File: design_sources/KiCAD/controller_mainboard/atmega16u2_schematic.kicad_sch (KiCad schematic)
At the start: 24 parts, among them J17 01x05_Socket, J18 02x02_pinheader, J19 02x03_pinheader, U2 ATmega16U2-M, Y2 16MHz

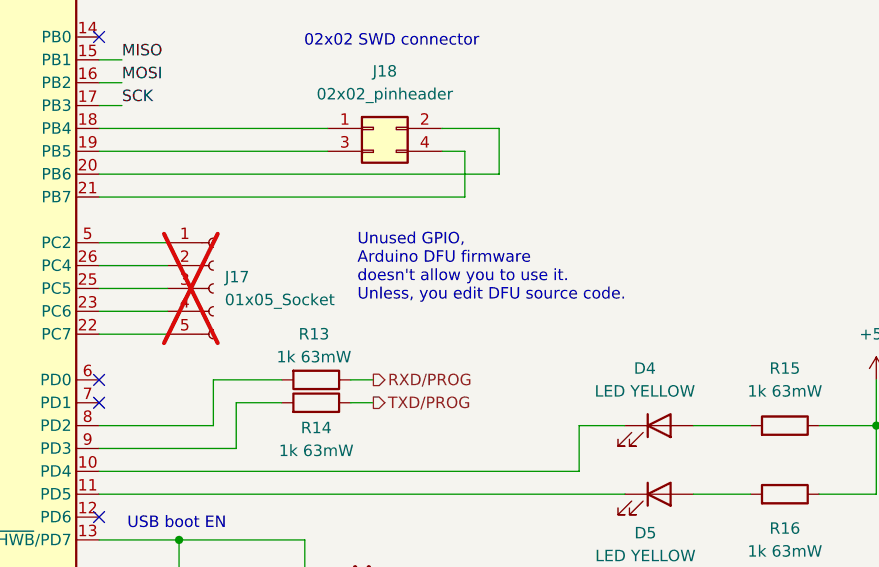
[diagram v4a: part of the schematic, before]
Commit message: Slight schematic adjustments and continue on draft pcb layout
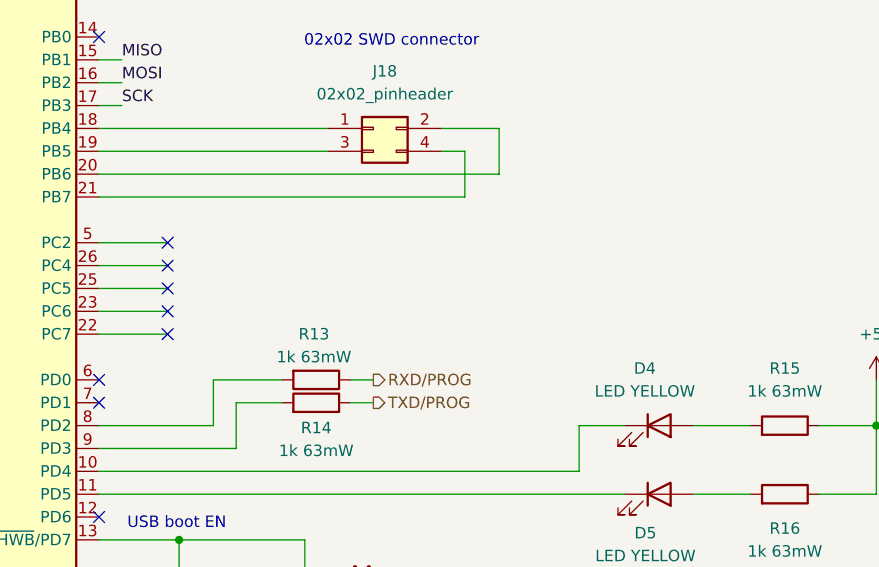
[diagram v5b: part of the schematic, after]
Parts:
- removed J17: 01x05_Socket, Connector_PinSocket_2.54mm:PinSocket_1x05_P2.54mm_Vertical, symbol Connector:Conn_01x05_Socket
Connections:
- no-connect marks 4 -> 9
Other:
- note removed: "Unused GPIO, Arduino DFU firmware doesn't allow you to use it. Unless, you edit DFU source code."
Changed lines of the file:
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@@
-		)
-	)
-	(text "Unused GPIO,\nArduino DFU firmware \ndoesn't allow you to use it.\nUnless, you edit DFU source code."
-		(exclude_from_sim no)
-		(at 148.082 96.774 0)
-		(effects
-			(font
-				(size 1.27 1.27)
-			)
-			(justify left)
 		)
 	)
@@
 	)
 	(no_connect
+		(at 127 101.6)
+	)
+	(no_connect
+		(at 127 93.98)
+	)
+	(no_connect
 		(at 119.38 124.46)
+	)
+	(no_connect
+		(at 127 104.14)
+	)
+	(no_connect
+		(at 127 96.52)
+	)
+	(no_connect
+		(at 127 99.06)
 	)
 	(wire
@@
 					(unit 1)
 				)
-			)
-		)
-	)
-	(symbol
-		(lib_id "Connector:Conn_01x05_Socket")
-		(at 132.08 99.06 0)
-		(unit 1)
-		(exclude_from_sim yes)
-		(in_bom no)
-		(on_board yes)
-		(dnp yes)
-		(fields_autoplaced yes)
-		(property "Reference" "J17"
-			(at 133.35 97.7899 0)
-			(effects
-				(font
-					(size 1.27 1.27)
-				)
-				(justify left)
-			)
-		)
-		(property "Value" "01x05_Socket"
-			(at 133.35 100.3299 0)
-			(effects
-				(font
-					(size 1.27 1.27)
-				)
-				(justify left)
-			)
-		)
-		(property "Footprint" "Connector_PinSocket_2.54mm:PinSocket_1x05_P2.54mm_Vertical"
-			(at 132.08 99.06 0)
-			(effects
-				(font
-					(size 1.27 1.27)
-				)
-				(hide yes)
-			)
-		)
-		(property "Datasheet" "~"
-			(at 132.08 99.06 0)
-			(effects
-				(font
-					(size 1.27 1.27)
-				)
-				(hide yes)
-			)
-		)
-		(property "Description" "Generic connector, single row, 01x05, script generated"
-			(at 132.08 99.06 0)
-			(effects
-				(font
-					(size 1.27 1.27)
-				)
-				(hide yes)
-			)
-		)
-		(pin "5"
-		)
-		(pin "4"
-		)
-		(pin "3"
-		)
-		(pin "2"
-		)
-		(pin "1"
-		)
-		(instances
-			(project ""
-				(path "/0fdfffec-3d24-4249-8ba9-dae7a6ccc250/56a5a4f6-b055-4ffd-8e95-057054573d13"
-					(reference "J17")
-					(unit 1)
-				)

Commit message: Advanced the hardware layout further.
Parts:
- added C93: 50V 22pF C0G, Capacitor_SMD:C_0402_1005Metric, symbol Device:C
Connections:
- net GND: now also C93.1
- net ~{RESET}: now also C93.2
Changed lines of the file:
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@@
+	(wire
+		(pts
+			(xy 199.39 54.61) (xy 199.39 52.07)
+		)
+		(stroke
+			(width 0)
+			(type default)
+		)
+	)
 	(wire
 		(pts
@@
 		(pts
 			(xy 199.39 121.92) (xy 205.74 121.92)
+		)
+		(stroke
+			(width 0)
+			(type default)
+		)
+	)
+	(wire
+		(pts
+			(xy 199.39 67.31) (xy 199.39 62.23)
 		)
 		(stroke
@@
 	(symbol
 		(lib_id "Device:C")
+		(at 199.39 58.42 180)
+		(unit 1)
+		(exclude_from_sim no)
+		(in_bom yes)
+		(on_board yes)
+		(dnp no)
+		(fields_autoplaced yes)
+		(property "Reference" "C93"
+			(at 195.58 57.1499 0)
+			(effects
+				(font
+					(size 1.27 1.27)
+				)
+				(justify left)
+			)
+		)
+		(property "Value" "50V 22pF C0G"
+			(at 195.58 59.6899 0)
+			(effects
+				(font
+					(size 1.27 1.27)
+				)
+				(justify left)
+			)
+		)
+		(property "Footprint" "Capacitor_SMD:C_0402_1005Metric"
+			(at 198.4248 54.61 0)
+			(effects
+				(font
+					(size 1.27 1.27)
+				)
+				(hide yes)
+			)
+		)
+		(property "Datasheet" "https://jlcpcb.com/api/file/downloadByFileSystemAccessId/8579707297419231232"
+			(at 199.39 58.42 0)
+			(effects
+				(font
+					(size 1.27 1.27)
+				)
+				(hide yes)
+			)
+		)
+		(property "Description" "Unpolarized capacitor"
+			(at 199.39 58.42 0)
+			(effects
+				(font
+					(size 1.27 1.27)
+				)
+				(hide yes)
+			)
+		)
+		(property "JLCPCB" "C1555"
+			(at 199.39 58.42 90)
+			(effects
+				(font
+					(size 1.27 1.27)
+				)
+				(hide yes)
+			)
+		)
+		(pin "2"
+		)
+		(pin "1"
+		)
+		(instances
+			(project "controller_mainboard"
+				(path "/0fdfffec-3d24-4249-8ba9-dae7a6ccc250/56a5a4f6-b055-4ffd-8e95-057054573d13"
+					(reference "C93")
+					(unit 1)
+				)
+			)
+		)
+	)
+	(symbol
+		(lib_id "Device:C")
 		(at 88.9 142.24 0)
 		(mirror x)
@@
 					(unit 1)
 				)
+			)
+		)
+	)
+	(symbol
+		(lib_id "power:GND")
+		(at 199.39 67.31 0)
+		(unit 1)
+		(exclude_from_sim no)
+		(in_bom yes)
+		(on_board yes)
+		(dnp no)
+		(fields_autoplaced yes)
+		(property "Reference" "#PWR0133"
+			(at 199.39 73.66 0)
+			(effects
+				(font
+					(size 1.27 1.27)
+				)
+				(hide yes)
+			)
+		)
+		(property "Value" "GND"
+			(at 199.39 72.39 0)
+			(effects
+				(font
+					(size 1.27 1.27)
+				)
+				(hide yes)
+			)
+		)
+		(property "Footprint" ""
+			(at 199.39 67.31 0)
+			(effects
+				(font
+					(size 1.27 1.27)
+				)
+				(hide yes)
+			)
+		)
+		(property "Datasheet" ""
+			(at 199.39 67.31 0)
+			(effects
+				(font
+					(size 1.27 1.27)
+				)
+				(hide yes)
+			)
+		)
+		(property "Description" "Power symbol creates a global label with name \"GND\" , ground"
+			(at 199.39 67.31 0)
+			(effects
+				(font
+					(size 1.27 1.27)
+				)
+				(hide yes)
+			)
+		)
+		(pin "1"
+		)
+		(instances
+			(project "controller_mainboard"
+				(path "/0fdfffec-3d24-4249-8ba9-dae7a6ccc250/56a5a4f6-b055-4ffd-8e95-057054573d13"
+					(reference "#PWR0133")
+					(unit 1)
+				)

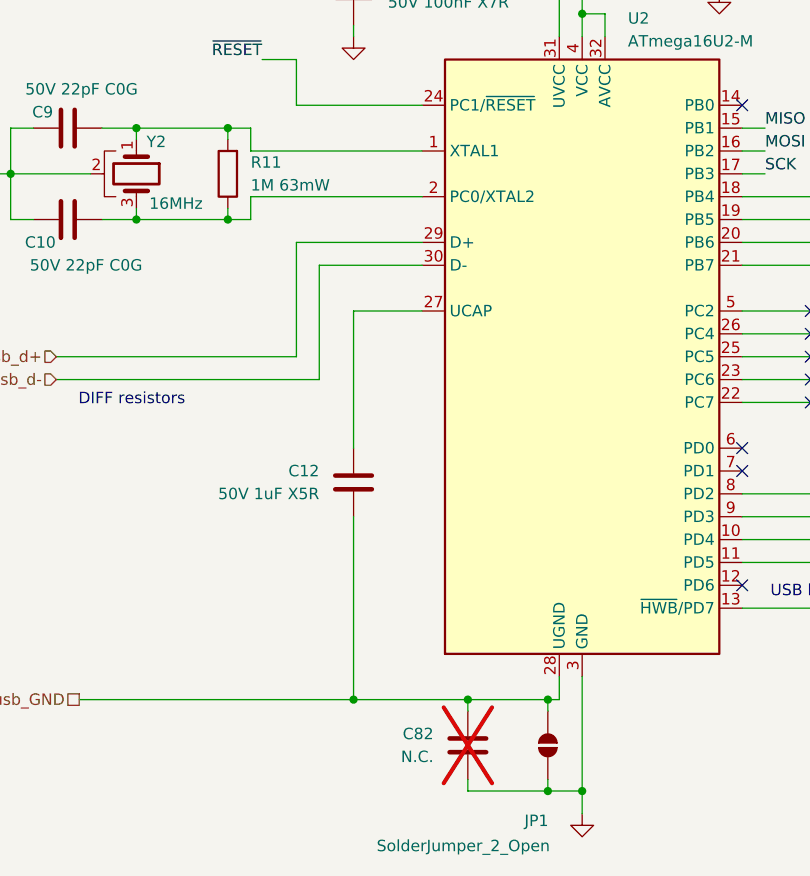
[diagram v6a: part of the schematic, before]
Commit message: Re-checked DRC, differing footprint warnings are fine, added production files for JLC placement and prod. TODO, maybe cool silk art at the bottom and definitive order list.
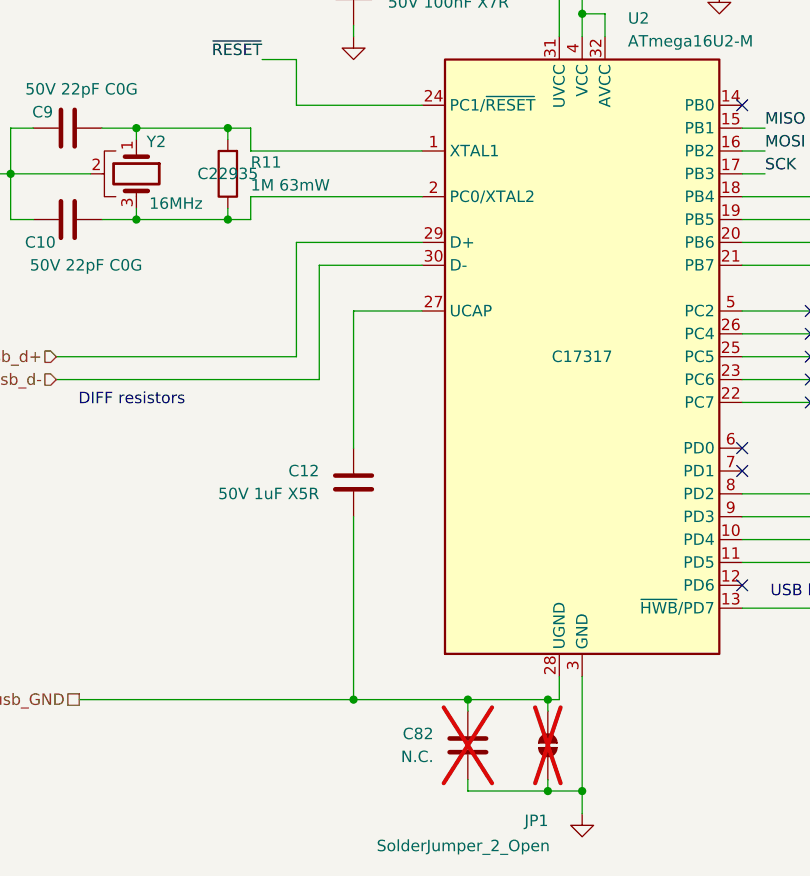
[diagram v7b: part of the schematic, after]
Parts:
- JP1: now not fitted
- R11: JLCPCB (none) -> C22935
- U2: JLCPCB (none) -> C17317
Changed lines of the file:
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@@
 		(in_bom no)
 		(on_board yes)
-		(dnp no)
+		(dnp yes)
 		(property "Reference" "JP1"
 			(at 96.52 150.622 90)
@@
 			)
 		)
+		(property "JLCPCB" "C22935"
+			(at 62.23 78.74 0)
+			(effects
+				(font
+					(size 1.27 1.27)
+				)
+			)
+		)
 		(pin "1"
 		)
@@
 			)
 		)
+		(property "JLCPCB" "C17317"
+			(at 101.6 99.06 0)
+			(effects
+				(font
+					(size 1.27 1.27)
+				)
+			)
+		)

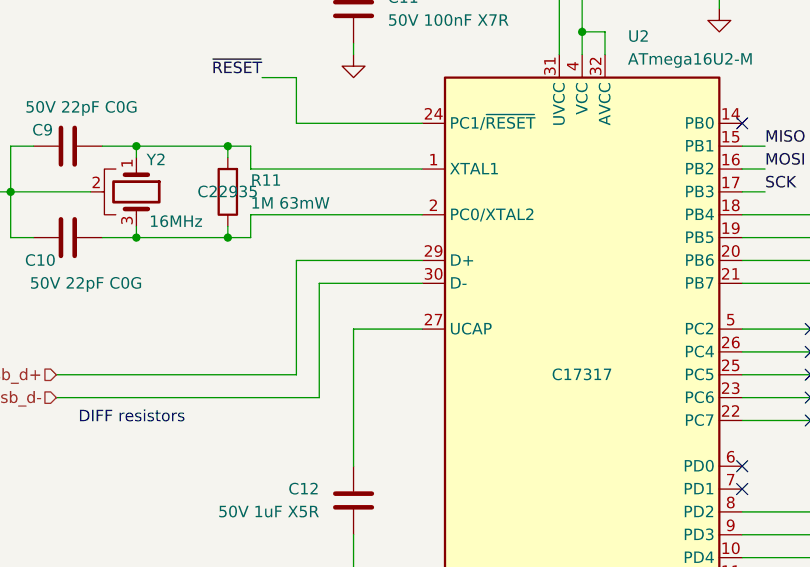
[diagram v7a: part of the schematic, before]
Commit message: Changed JLCPCB field to LCSC
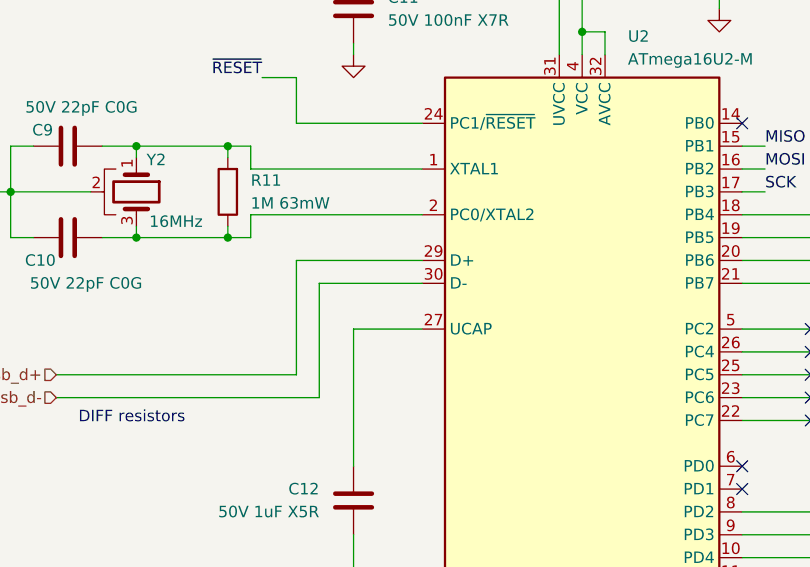
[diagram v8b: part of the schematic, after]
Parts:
- C10, C9, C93: JLCPCB C1555 -> (none); LCSC (none) -> C1555
- C11, C13, C15: JLCPCB C14663 -> (none); LCSC (none) -> C14663
- C12, C14: JLCPCB C15849 -> (none); LCSC (none) -> C15849
- D4, D5: JLCPCB C72038 -> (none); LCSC (none) -> C72038
- D6: JLCPCB C22452 -> (none); LCSC (none) -> C22452
- R11: JLCPCB C22935 -> (none); LCSC (none) -> C22935
- R12, R13, R14, R15, R16: JLCPCB C11702 -> (none); LCSC (none) -> C11702
- R17: JLCPCB C25744 -> (none); LCSC (none) -> C25744
- U2: JLCPCB C17317 -> (none); LCSC (none) -> C17317
- Y2: JLCPCB C783275 -> (none); LCSC (none) -> C783275
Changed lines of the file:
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@@
 			)
 		)
-		(property "JLCPCB" "C22452"
+		(property "LCSC" "C22452"
 			(at 182.88 44.45 90)
 			(effects
@@
 			)
 		)
-		(property "JLCPCB" "C14663"
+		(property "LCSC" "C14663"
 			(at 76.2 58.42 0)
 			(effects
@@
 			)
 		)
-		(property "JLCPCB" "C11702"
-			(at 143.51 111.76 0)
+		(property "LCSC" "C11702"
+			(at 143.51 111.76 90)
 			(effects
 				(font
@@
 			)
 		)
-		(property "JLCPCB" "C11702"
+		(property "LCSC" "C11702"
 			(at 128.27 134.62 0)
 			(effects
@@
 			)
 		)
-		(property "JLCPCB" "C783275"
+		(property "LCSC" "C783275"
 			(at 52.07 78.74 90)
 			(effects
@@
 			)
 		)
-		(property "JLCPCB" "C1555"
-			(at 199.39 58.42 90)
+		(property "LCSC" "C1555"
+			(at 199.39 58.42 0)
 			(effects
 				(font
@@
 			)
 		)
-		(property "JLCPCB" "C72038"
+		(property "LCSC" "C72038"
 			(at 181.61 121.92 0)
 			(effects
@@
 			)
 		)
-		(property "JLCPCB" "C14663"
-			(at 110.49 46.99 0)
+		(property "LCSC" "C14663"
+			(at 110.49 46.99 90)
 			(effects
 				(font
@@
 			)
 		)
-		(property "JLCPCB" "C1555"
+		(property "LCSC" "C1555"
 			(at 44.45 73.66 90)
 			(effects
@@
 			)
 		)
-		(property "JLCPCB" "C15849"
-			(at 110.49 52.07 0)
+		(property "LCSC" "C15849"
+			(at 110.49 52.07 90)
 			(effects
 				(font
@@
 			)
 		)
-		(property "JLCPCB" "C15849"
+		(property "LCSC" "C15849"
 			(at 76.2 113.03 0)
 			(effects
@@
 			)
 		)
-		(property "JLCPCB" "C11702"
-			(at 143.51 109.22 0)
+		(property "LCSC" "C11702"
+			(at 143.51 109.22 90)
 			(effects
 				(font
@@
 			)
 		)
-		(property "JLCPCB" "C1555"
+		(property "LCSC" "C1555"
 			(at 44.45 83.82 90)
 			(effects
@@
 			)
 		)
-		(property "JLCPCB" "C22935"
+		(property "LCSC" "C22935"
 			(at 62.23 78.74 0)
 			(effects
@@
 					(size 1.27 1.27)
 				)
+				(hide yes)
 			)
 		)
@@
 			)
 		)
-		(property "JLCPCB" "C72038"
+		(property "LCSC" "C72038"
 			(at 181.61 114.3 0)
 			(effects
@@
 			)
 		)
-		(property "JLCPCB" "C25744"
+		(property "LCSC" "C25744"
 			(at 199.39 44.45 0)
 			(effects
@@
 			)
 		)
-		(property "JLCPCB" "C11702"
-			(at 195.58 114.3 0)
+		(property "LCSC" "C11702"
+			(at 195.58 114.3 90)
 			(effects
 				(font
@@
 			)
 		)
-		(property "JLCPCB" "C14663"
-			(at 148.59 132.08 0)
+		(property "LCSC" "C14663"
+			(at 148.59 132.08 90)
 			(effects
 				(font
@@
 			)
 		)
-		(property "JLCPCB" "C11702"
-			(at 195.58 121.92 0)
+		(property "LCSC" "C11702"
+			(at 195.58 121.92 90)
 			(effects
 				(font
@@
 			)
 		)
-		(property "JLCPCB" "C17317"
+		(property "LCSC" "C17317"
 			(at 101.6 99.06 0)
 			(effects
@@
 					(size 1.27 1.27)
 				)
-			)
-		)
+				(hide yes)
+			)
+		)
